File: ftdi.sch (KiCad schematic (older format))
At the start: 31 parts

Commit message: initial footprint assignment and VERY rough placement
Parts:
- C201, C202, C203, C204, C205, C206, C207, C208: renamed from C?; footprint (none) -> Capacitor_SMD:C_0402_1005Metric
- R201, R202, R203, R204, R205, R206, R207, R208, R209, R210, R211, R212, R213, R214, R215, R216, R217, R218, R219, R220: renamed from R?; footprint (none) -> Resistor_SMD:R_0402_1005Metric
- U201: renamed from U?; value 93LCxxC -> 93LC56C-I/SN; footprint (none) -> Package_SO:SOIC-8_3.9x4.9mm_P1.27mm
- U202: renamed from U?; footprint (none) -> Package_QFP:LQFP-64_10x10mm_P0.5mm
- gave numbers to parts that had none: 1

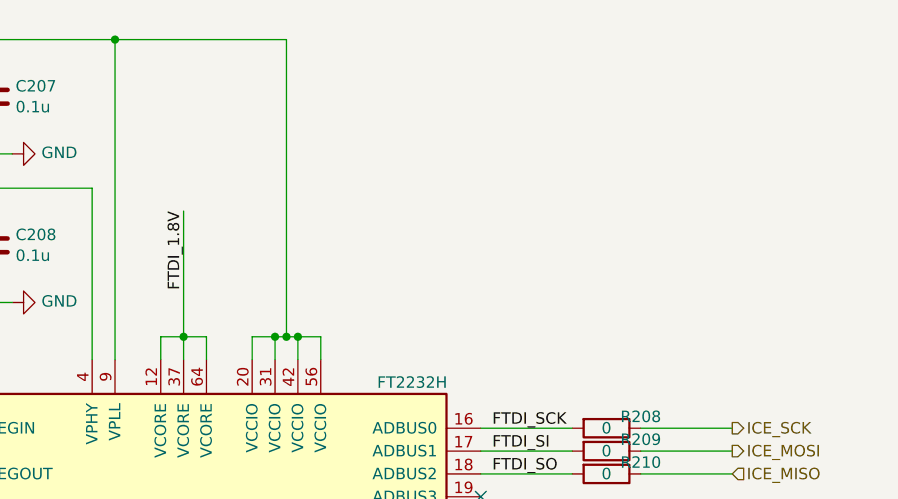
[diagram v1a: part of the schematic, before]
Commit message: local component placement
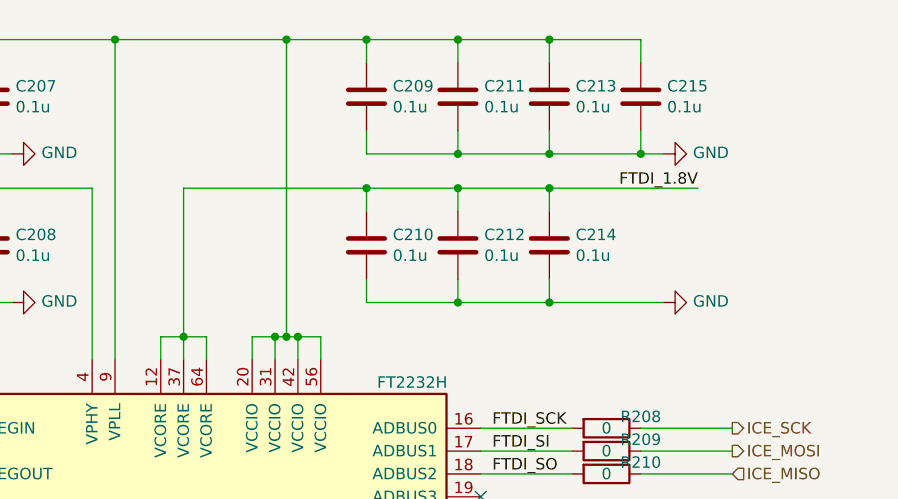
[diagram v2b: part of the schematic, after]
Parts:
- added C209, C210, C211, C212, C213, C214, C215: 0.1u, Capacitor_SMD:C_0402_1005Metric, symbol Device:C
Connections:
- net 3.3v: now also C209.1, C211.1, C213.1, C215.1
- net FTDI_1.8V: now also C210.1, C212.1, C214.1
- net GND: now also C209.2, C210.2, C211.2, C212.2, C213.2, C214.2, C215.2
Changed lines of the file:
@@
 	2000 2950 2500 2950
 Connection ~ 2500 2950
-Text Label 4700 1800 3    50   ~ 0
+Text Label 6950 1700 2    50   ~ 0
 FTDI_1.8V
 Wire Wire Line
@@
 Wire Wire Line
 	4700 2350 4600 2350
-Wire Wire Line
-	4700 2350 4700 1800
 $Comp
 L Device:R R207
@@
 Text HLabel 7100 5150 2    50   Input ~ 0
 FTDI_DCD
+$Comp
+L Device:C C209
+U 1 1 5DFF5B79
+P 5500 1300
+F 0 "C209" H 5615 1346 50  0000 L CNN
+F 1 "0.1u" H 5615 1255 50  0000 L CNN
+F 2 "Capacitor_SMD:C_0402_1005Metric" H 5538 1150 50  0001 C CNN
+F 3 "~" H 5500 1300 50  0001 C CNN
+	1    5500 1300
+	1    0    0    -1
+$EndComp
+$Comp
+L Device:C C211
+U 1 1 5DFF7BB1
+P 5900 1300
+F 0 "C211" H 6015 1346 50  0000 L CNN
+F 1 "0.1u" H 6015 1255 50  0000 L CNN
+F 2 "Capacitor_SMD:C_0402_1005Metric" H 5938 1150 50  0001 C CNN
+F 3 "~" H 5900 1300 50  0001 C CNN
+	1    5900 1300
+	1    0    0    -1
+$EndComp
+$Comp
+L Device:C C213
+U 1 1 5DFF7ED1
+P 6300 1300
+F 0 "C213" H 6415 1346 50  0000 L CNN
+F 1 "0.1u" H 6415 1255 50  0000 L CNN
+F 2 "Capacitor_SMD:C_0402_1005Metric" H 6338 1150 50  0001 C CNN
+F 3 "~" H 6300 1300 50  0001 C CNN
+	1    6300 1300
+	1    0    0    -1
+$EndComp
+$Comp
+L Device:C C215
+U 1 1 5DFF87D2
+P 6700 1300
+F 0 "C215" H 6815 1346 50  0000 L CNN
+F 1 "0.1u" H 6815 1255 50  0000 L CNN
+F 2 "Capacitor_SMD:C_0402_1005Metric" H 6738 1150 50  0001 C CNN
+F 3 "~" H 6700 1300 50  0001 C CNN
+	1    6700 1300
+	1    0    0    -1
+$EndComp
+$Comp
+L power:GND #PWR0208
+U 1 1 5DFF8E57
+P 6800 1550
+F 0 "#PWR0208" H 6800 1300 50  0001 C CNN
+F 1 "GND" V 6805 1422 50  0000 R CNN
+F 2 "" H 6800 1550 50  0001 C CNN
+F 3 "" H 6800 1550 50  0001 C CNN
+	1    6800 1550
+	0    -1   -1   0
+$EndComp
+Wire Wire Line
+	6800 1550 6700 1550
+Wire Wire Line
+	5500 1550 5500 1450
+Wire Wire Line
+	5900 1450 5900 1550
+Connection ~ 5900 1550
+Wire Wire Line
+	5900 1550 5500 1550
+Wire Wire Line
+	6300 1550 6300 1450
+Connection ~ 6300 1550
+Wire Wire Line
+	6300 1550 5900 1550
+Wire Wire Line
+	6700 1450 6700 1550
+Connection ~ 6700 1550
+Wire Wire Line
+	6700 1550 6300 1550
+Wire Wire Line
+	6700 1150 6700 1050
+Wire Wire Line
+	6700 1050 6300 1050
+Connection ~ 5150 1050
+Wire Wire Line
+	5500 1150 5500 1050
+Connection ~ 5500 1050
+Wire Wire Line
+	5500 1050 5150 1050
+Wire Wire Line
+	5900 1050 5900 1150
+Connection ~ 5900 1050
+Wire Wire Line
+	5900 1050 5500 1050
+Wire Wire Line
+	6300 1150 6300 1050
+Connection ~ 6300 1050
+Wire Wire Line
+	6300 1050 5900 1050
+$Comp
+L Device:C C210
+U 1 1 5E0323EA
+P 5500 1950
+F 0 "C210" H 5615 1996 50  0000 L CNN
+F 1 "0.1u" H 5615 1905 50  0000 L CNN
+F 2 "Capacitor_SMD:C_0402_1005Metric" H 5538 1800 50  0001 C CNN
+F 3 "~" H 5500 1950 50  0001 C CNN
+	1    5500 1950
+	1    0    0    -1
+$EndComp
+Wire Wire Line
+	4700 1700 5500 1700
+Wire Wire Line
+	4700 1700 4700 2350
+Wire Wire Line
+	5500 1800 5500 1700
+Connection ~ 5500 1700
+Wire Wire Line
+	5500 1700 5900 1700
+$Comp
+L Device:C C212
+U 1 1 5E06C91C
+P 5900 1950
+F 0 "C212" H 6015 1996 50  0000 L CNN
+F 1 "0.1u" H 6015 1905 50  0000 L CNN
+F 2 "Capacitor_SMD:C_0402_1005Metric" H 5938 1800 50  0001 C CNN
+F 3 "~" H 5900 1950 50  0001 C CNN
+	1    5900 1950
+	1    0    0    -1
+$EndComp
+$Comp
+L Device:C C214
+U 1 1 5E06CC60
+P 6300 1950
+F 0 "C214" H 6415 1996 50  0000 L CNN
+F 1 "0.1u" H 6415 1905 50  0000 L CNN
+F 2 "Capacitor_SMD:C_0402_1005Metric" H 6338 1800 50  0001 C CNN
+F 3 "~" H 6300 1950 50  0001 C CNN
+	1    6300 1950
+	1    0    0    -1
+$EndComp
+Wire Wire Line
+	6300 1800 6300 1700
+Connection ~ 6300 1700
+Wire Wire Line
+	6300 1700 6950 1700
+Wire Wire Line
+	5900 1700 5900 1800
+Connection ~ 5900 1700
+Wire Wire Line
+	5900 1700 6300 1700
+Wire Wire Line
+	5500 2100 5500 2200
+Wire Wire Line
+	5500 2200 5900 2200
+$Comp
+L power:GND #PWR0209
+U 1 1 5E0855D9
+P 6800 2200
+F 0 "#PWR0209" H 6800 1950 50  0001 C CNN
+F 1 "GND" V 6805 2072 50  0000 R CNN
+F 2 "" H 6800 2200 50  0001 C CNN
+F 3 "" H 6800 2200 50  0001 C CNN
+	1    6800 2200
+	0    -1   -1   0
+$EndComp
+Wire Wire Line
+	6300 2200 6300 2100
+Connection ~ 6300 2200
+Wire Wire Line
+	6300 2200 6800 2200
+Wire Wire Line
+	5900 2100 5900 2200
+Connection ~ 5900 2200
+Wire Wire Line
+	5900 2200 6300 2200
 $EndSCHEMATC

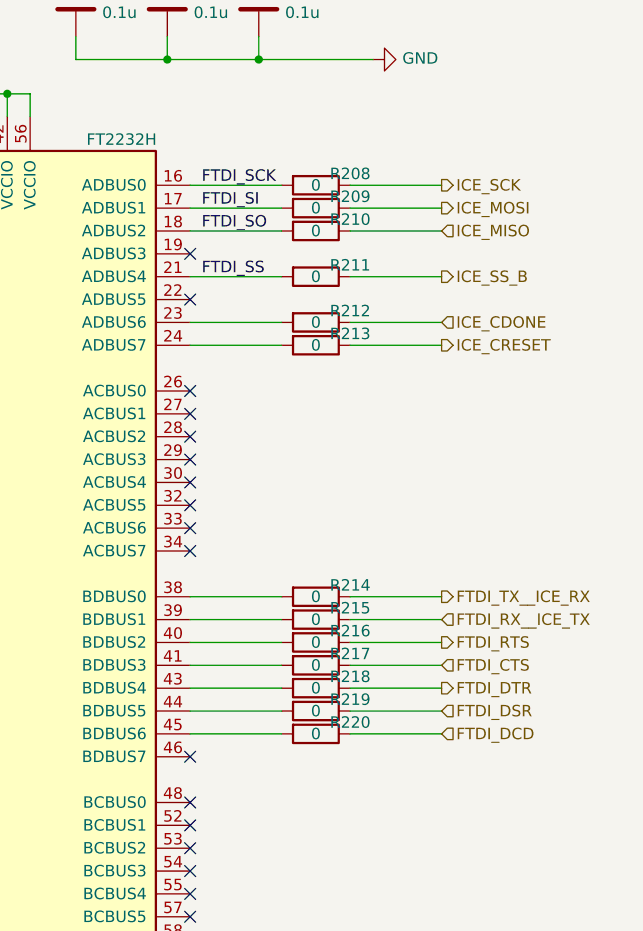
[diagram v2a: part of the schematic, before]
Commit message: assigning pins, adding test points, placing stuff, etc
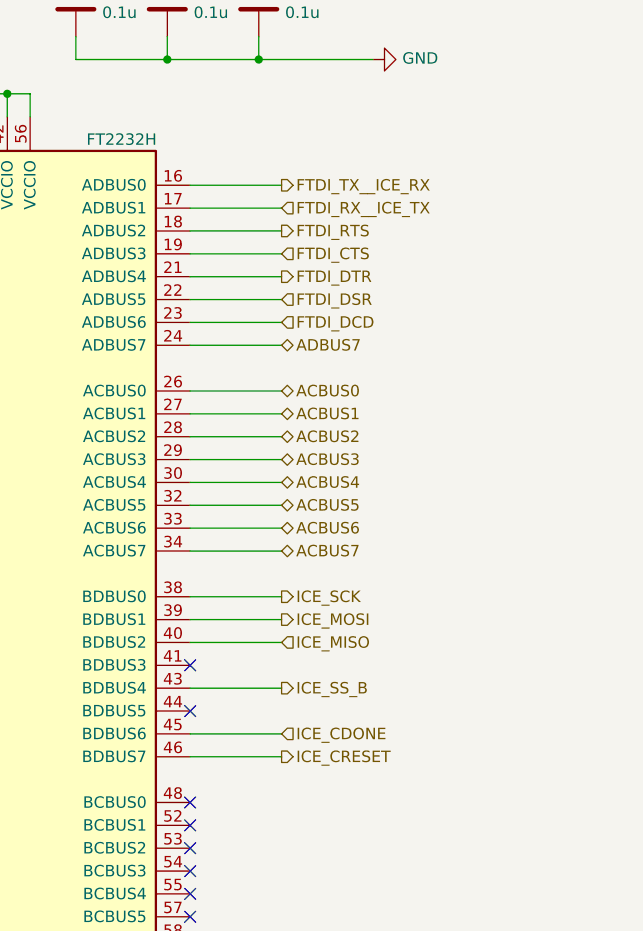
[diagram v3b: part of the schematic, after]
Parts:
- removed R208, R209, R210, R211, R212, R213, R214, R215, R216, R217, R218, R219, R220: 0, Resistor_SMD:R_0402_1005Metric, symbol Device:R
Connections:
- net FTDI_SCK is gone; now on net FTDI_TX__ICE_RX: U202.16 (ADBUS0)
- net FTDI_SI is gone; now on net FTDI_RX__ICE_TX: U202.17 (ADBUS1)
- net FTDI_SO is gone; now on net FTDI_RTS: U202.18 (ADBUS2)
- net FTDI_SS is gone; now on net FTDI_DTR: U202.21 (ADBUS4)
- net FTDI_CTS: now also U202.19 (ADBUS3)
- net FTDI_DCD: now also U202.23 (ADBUS6)
- net FTDI_DSR: now also U202.22 (ADBUS5)
- net ICE_CDONE: now also U202.45 (BDBUS6)
- net ICE_CRESET: now also U202.46 (BDBUS7)
- net ICE_MISO: now also U202.40 (BDBUS2)
- net ICE_MOSI: now also U202.39 (BDBUS1)
- net ICE_SCK: now also U202.38 (BDBUS0)
- net ICE_SS_B: now also U202.43 (BDBUS4)
- net ADBUS7: now reaches U202.24 (ADBUS7)
- net ACBUS0: now reaches U202.26 (ACBUS0)
- net ACBUS1: now reaches U202.27 (ACBUS1)
- net ACBUS2: now reaches U202.28 (ACBUS2)
- net ACBUS3: now reaches U202.29 (ACBUS3)
- net ACBUS4: now reaches U202.30 (ACBUS4)
- net ACBUS5: now reaches U202.32 (ACBUS5)
- net ACBUS6: now reaches U202.33 (ACBUS6)
- net ACBUS7: now reaches U202.34 (ACBUS7)
- no-connect marks 22 -> 13
